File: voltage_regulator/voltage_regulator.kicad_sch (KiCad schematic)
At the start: 19 parts, among them J1 Conn_01x05_Male, U1 TPS54331DR

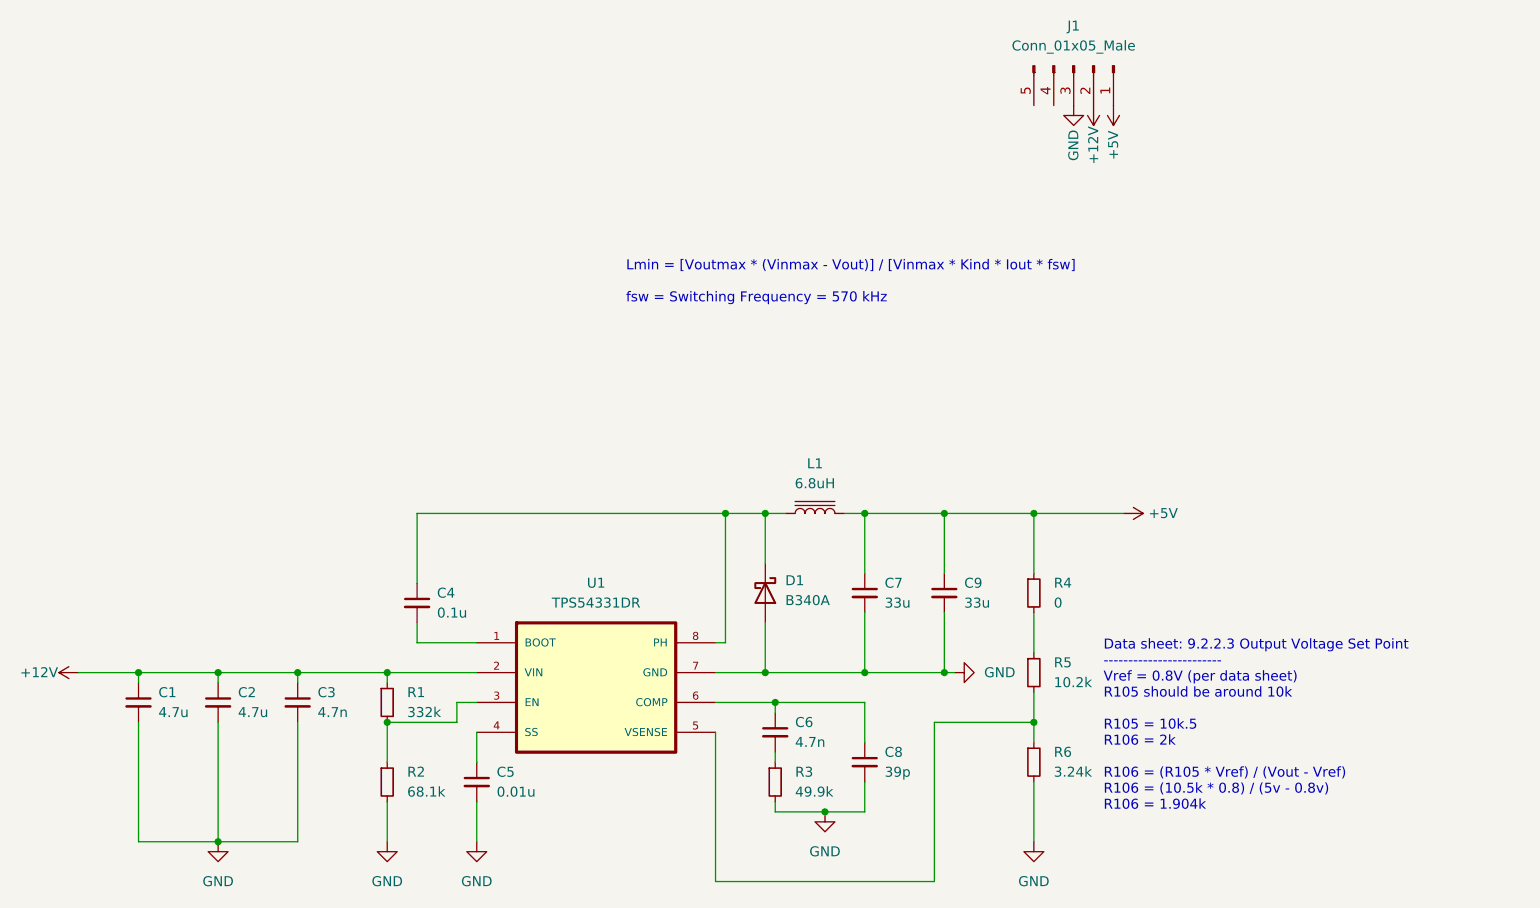
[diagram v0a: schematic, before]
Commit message: Updated layout
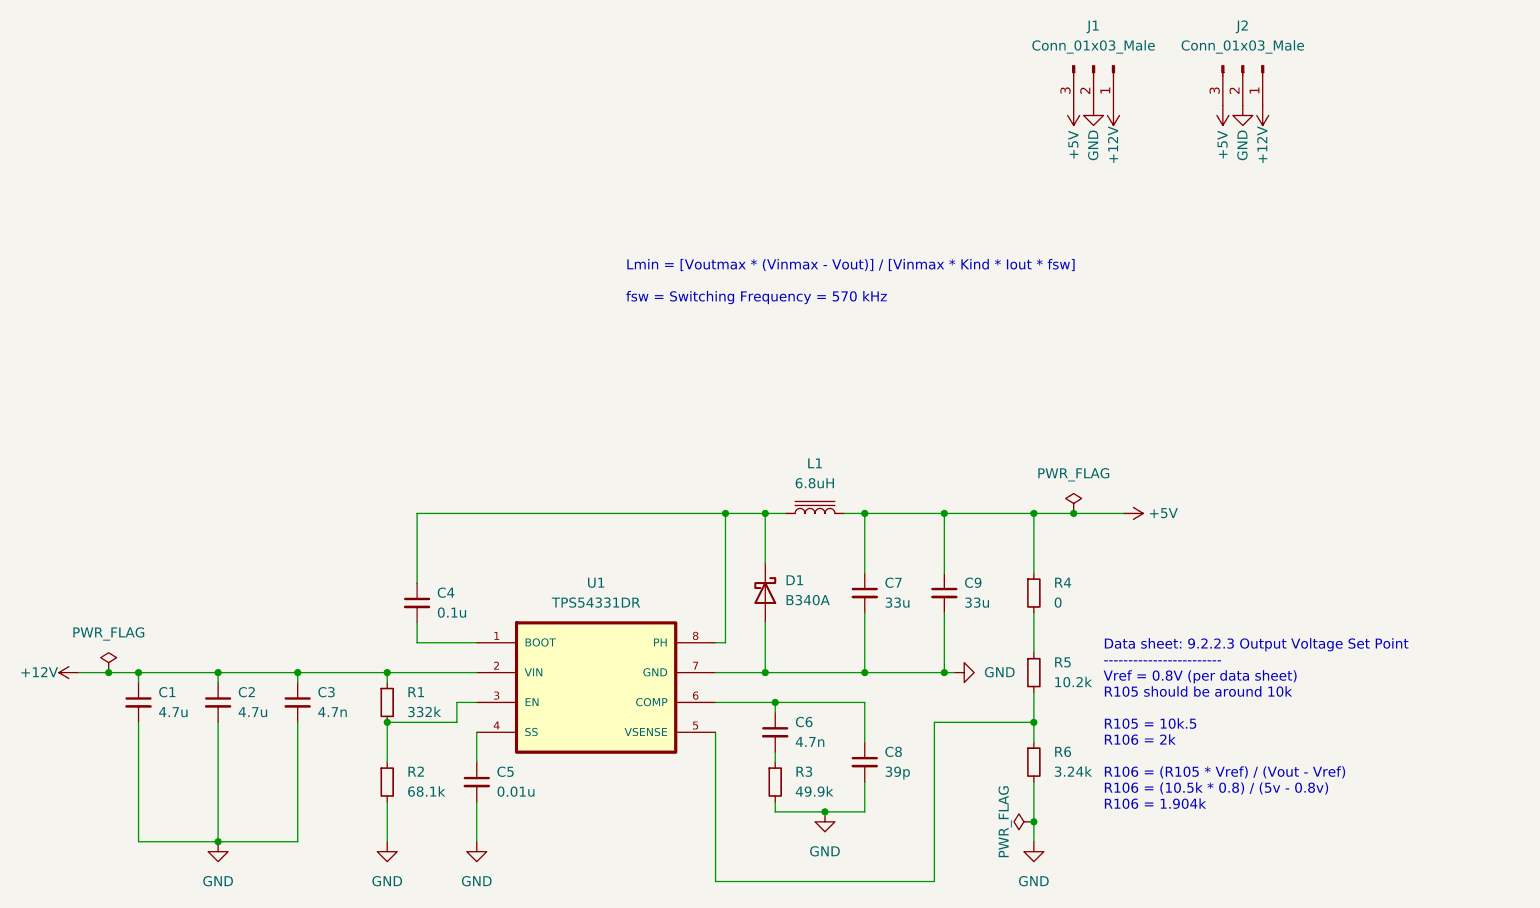
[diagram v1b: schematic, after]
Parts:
- added J2: Conn_01x03_Male, Connector_PinHeader_2.54mm:PinHeader_1x03_P2.54mm_Vertical, symbol Connector:Conn_01x03_Male
- J1: value Conn_01x05_Male -> Conn_01x03_Male; footprint Connector_PinSocket_2.54mm:PinSocket_1x05_P2.54mm_Vertical -> Connector_PinHeader_2.54mm:PinHeader_1x03_P2.54mm_Vertical; symbol Connector:Conn_01x05_Male -> Connector:Conn_01x03_Male
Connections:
- net +12V: now also J1.1 (Pin_1), J2.1 (Pin_1); no longer J1.2 (Pin_2)
- net +5V: now also J1.3 (Pin_3), J2.3 (Pin_3); no longer J1.1 (Pin_1)
- net GND: now also J1.2 (Pin_2), J2.2 (Pin_2); no longer J1.3 (Pin_3)
